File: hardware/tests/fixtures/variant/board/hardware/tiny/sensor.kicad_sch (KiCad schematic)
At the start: 3 parts

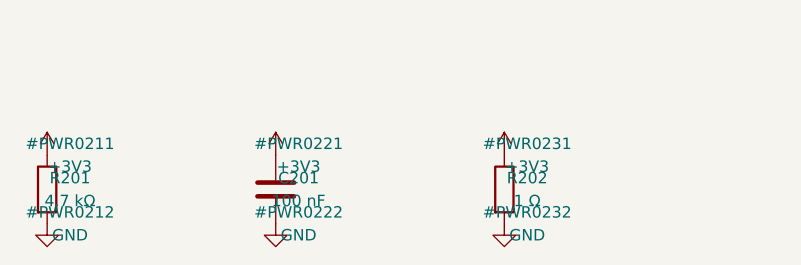
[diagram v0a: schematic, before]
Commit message: odapkit variant: absent-state check and software outputs per variant (RFC 0011 rules 2, 7, 8)
The absent-state check reads the XML netlist with the variant's resolution: every
net a dnp block touches is classified with the fitted parts only (single-pin,
floating, rail without source, defined) and matched to a declared absent state
from the block sheets' interface tables or the record's absent_state list; nets
touched only by other unfitted parts are reported when they become single-pin.
Findings absent.floating, absent.single-pin, absent.rail-unsourced,
absent.undeclared, absent.declared-mismatch and absent.not-applicable.

apply writes absent-state.json (opendap.variant-absent-state/v1),
software/capabilities.json (opendap.variant-capabilities/v1, a fragment for the
device description; consumer side open) and software/devicetree.json
(opendap.variant-devicetree/v1) with variant.dtso, status okay or disabled per
block node, blocks with no node listed as skipped. check runs the absent-state
check per variant. Block records gain structured absent_state and software;
the Markdown catalog reads its Absent state and Software rows. The fixture's
sensor sheet carries an interface table.

Co-Authored-By: Claude Opus 5.5 <noreply@anthropic.com>
Claude-Session: https://claude.ai/code/session_01Ei262h3TpgY9vyfNLMi5Mn
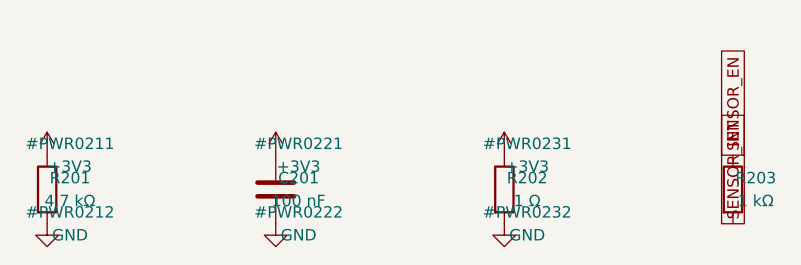
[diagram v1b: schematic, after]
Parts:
- added R203: 1 kΩ, Resistor_SMD:R_0603_1608Metric, symbol Device:R
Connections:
- new net SENSOR_EN: R203.1
- new net SENSOR_INT: R203.2
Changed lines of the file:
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@@
   (instances (project "tiny" (path "/66a81b00-37dd-53f5-81ba-daabee42749a/45e8c92c-d494-57f7-85bf-c9f7de86d5ef" (reference "#PWR0232") (unit 1))))
 )
+(symbol (lib_id "Device:R") (at 139.7 60.96 0) (unit 1) (body_style 1) (exclude_from_sim no) (in_bom yes) (on_board yes) (dnp no)
+  (property "Reference" "R203" (at 142.23999999999998 59.69 0) (effects (font (size 1.27 1.27))))
+  (property "Value" "1 kΩ" (at 142.23999999999998 62.230000000000004 0) (effects (font (size 1.27 1.27))))
+  (property "Footprint" "Resistor_SMD:R_0603_1608Metric" (at 139.7 60.96 0) (effects (font (size 1.27 1.27)) (hide yes)))
+  (property "Datasheet" "" (at 139.7 60.96 0) (effects (font (size 1.27 1.27)) (hide yes)))
+  (property "Block" "blk.sensor" (at 139.7 60.96 0) (effects (font (size 1.27 1.27)) (hide yes)))
+  (property "MPN" "RC0603FR-071KL" (at 139.7 60.96 0) (effects (font (size 1.27 1.27)) (hide yes)))
+  (property "Manufacturer" "YAGEO" (at 139.7 60.96 0) (effects (font (size 1.27 1.27)) (hide yes)))
+  (pin "1")
+  (pin "2")
+  (instances (project "tiny" (path "/66a81b00-37dd-53f5-81ba-daabee42749a/45e8c92c-d494-57f7-85bf-c9f7de86d5ef" (reference "R203") (unit 1))))
+)
+(global_label "SENSOR_EN" (shape passive) (at 139.7 57.15 90) (effects (font (size 1.27 1.27)) (justify left)))
+(global_label "SENSOR_INT" (shape passive) (at 139.7 64.77 90) (effects (font (size 1.27 1.27)) (justify left)))
+(table (column_count 3) (border (external yes) (header yes) (stroke (width 0) (type solid))) (separators (rows yes) (cols yes) (stroke (width 0) (type solid))) (column_widths 30.48 20.32 60.96) (row_heights 5.08 5.08 5.08) (cells (table_cell "Net" (exclude_from_sim no) (at 30.48 101.6 0) (size 30.48 5.08) (margins 0.9525 0.9525 0.9525 0.9525) (span 1 1) (fill (type none)) (effects (font (size 1.27 1.27) (bold yes)) (justify left top))) (table_cell "Direction" (exclude_from_sim no) (at 60.96 101.6 0) (size 20.32 5.08) (margins 0.9525 0.9525 0.9525 0.9525) (span 1 1) (fill (type none)) (effects (font (size 1.27 1.27) (bold yes)) (justify left top))) (table_cell "Absent state (block not fitted)" (exclude_from_sim no) (at 81.28 101.6 0) (size 60.96 5.08) (margins 0.9525 0.9525 0.9525 0.9525) (span 1 1) (fill (type none)) (effects (font (size 1.27 1.27) (bold yes)) (justify left top))) (table_cell "SENSOR_EN" (exclude_from_sim no) (at 30.48 106.68 0) (size 30.48 5.08) (margins 0.9525 0.9525 0.9525 0.9525) (span 1 1) (fill (type none)) (effects (font (size 1.27 1.27)) (justify left top))) (table_cell "Input" (exclude_from_sim no) (at 60.96 106.68 0) (size 20.32 5.08) (margins 0.9525 0.9525 0.9525 0.9525) (span 1 1) (fill (type none)) (effects (font (size 1.27 1.27)) (justify left top))) (table_cell "100 kΩ pull-down on blk.core: off" (exclude_from_sim no) (at 81.28 106.68 0) (size 60.96 5.08) (margins 0.9525 0.9525 0.9525 0.9525) (span 1 1) (fill (type none)) (effects (font (size 1.27 1.27)) (justify left top))) (table_cell "SENSOR_INT" (exclude_from_sim no) (at 30.48 111.76 0) (size 30.48 5.08) (margins 0.9525 0.9525 0.9525 0.9525) (span 1 1) (fill (type none)) (effects (font (size 1.27 1.27)) (justify left top))) (table_cell "Output" (exclude_from_sim no) (at 60.96 111.76 0) (size 20.32 5.08) (margins 0.9525 0.9525 0.9525 0.9525) (span 1 1) (fill (type none)) (effects (font (size 1.27 1.27)) (justify left top))) (table_cell "4.7 kΩ pull-up on blk.core" (exclude_from_sim no) (at 81.28 111.76 0) (size 60.96 5.08) (margins 0.9525 0.9525 0.9525 0.9525) (span 1 1) (fill (type none)) (effects (font (size 1.27 1.27)) (justify left top)))))
 (sheet_instances (path "/" (page "1")))
 )
